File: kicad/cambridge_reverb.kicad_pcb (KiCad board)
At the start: 2 copper layers, 190 x 115 mm, 113 parts, among them IC1 TL072CP, IC2 TL072CP, Q1 MMBF5457, Q2 MMBF5457, T1 reuse / AnTek AS-0524, U1 LM317T

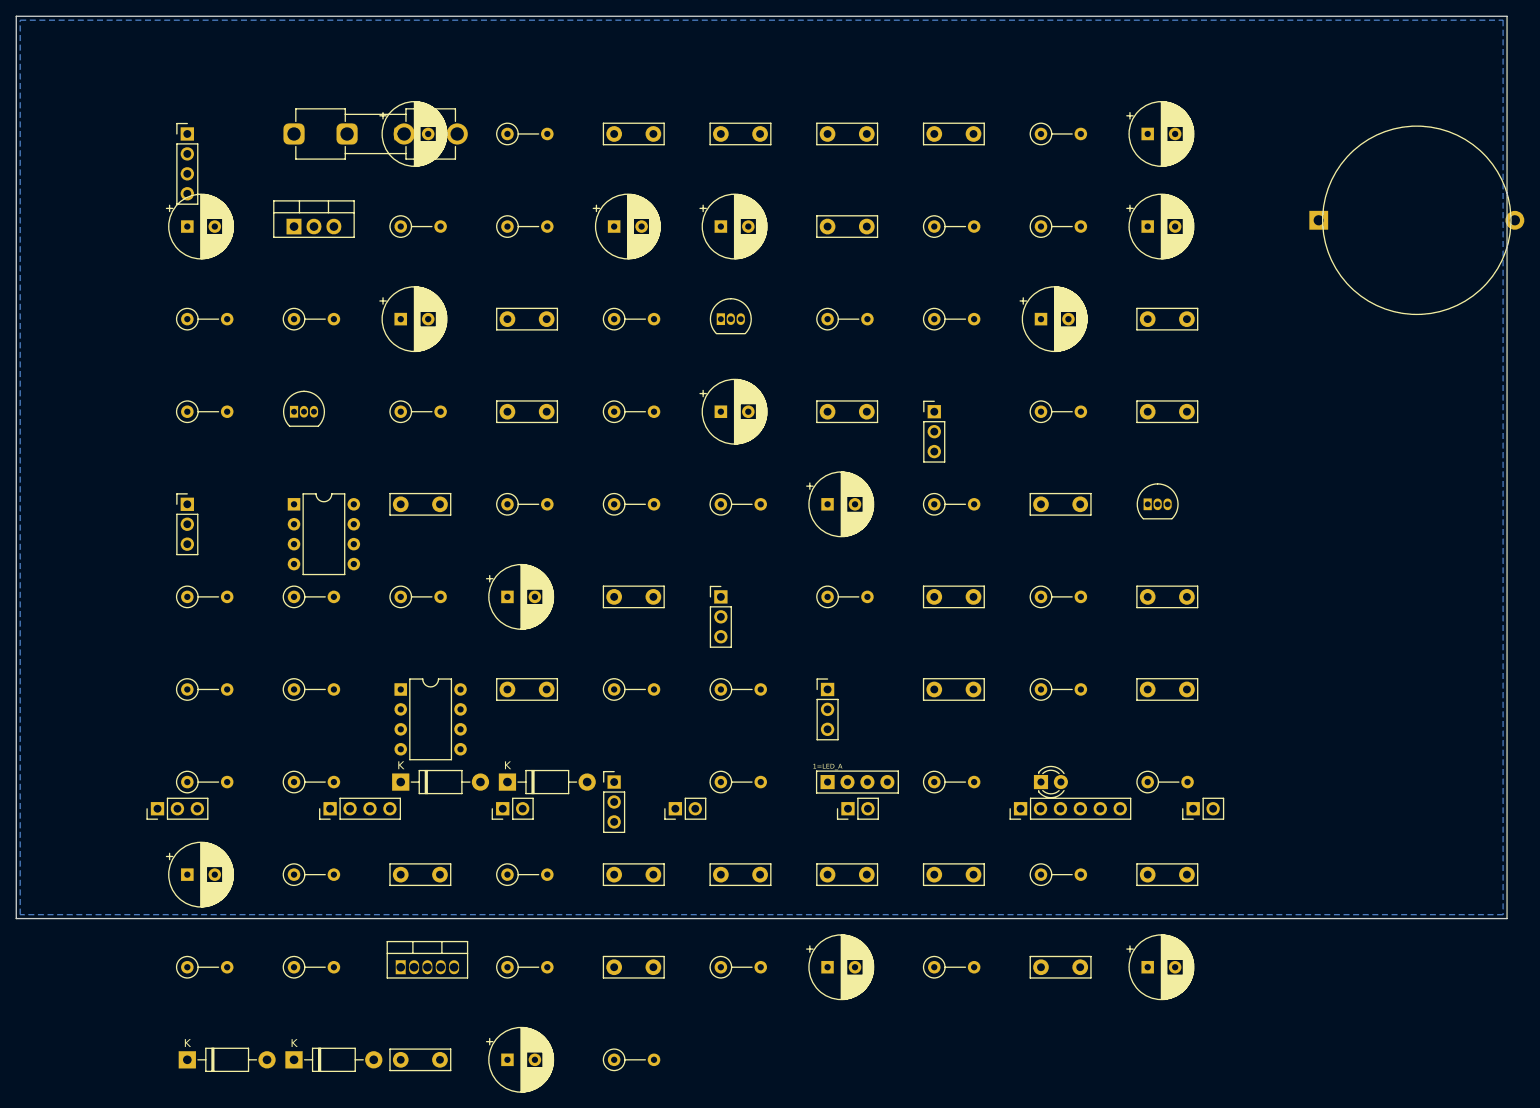
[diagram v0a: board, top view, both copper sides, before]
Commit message: Datasheet footprints, floor-plan placement, headless autoroute (144/145, DRC 0)
PCB-AUDIT s1 fixes with datasheet-derived project footprints:
- TO-220-5_Vertical_P1.70mm_LM1875 (TI NDH0005D): 1.45 mm pads on the 1.1 mm
  drill -> 0.175 mm annular (was 0.0875, 5 DRC errors); pad-local 0.2 mm clearance
- Bridge_KBP_P3.81mm (Diodes DS39310 KBP404G-KBP410G, pins + ~ ~ -); bridge
  symbol renumbered to the physical order; errata #3 updated (KBU needs a swap)
- value-aware CP/R sizing (real can sizes for 4700/2200/1000 uF, 5 W / 1 W
  resistors, fat pads on the 0R speaker return); Part 4 wire pads for all
  off-board wiring (2.0 mm/1.2 mm signal, 3.0 mm/1.5 mm speaker + transformer)
- VRAW/AC1/AC2 moved into the HighCurrent net class (errata #11)

gen_pcb.py now places to the Part 5 floor plan: balanced columns (Input/Preamp
with Tone stacked below | Reverb/Trem/MRB | Power Amp | PSU), signal order inside
zones with serpentine shelves, LM1875/LM317 on the top edge with the 10 mm
keep-out, wiring edge along the bottom, 4x M3 holes, two locked 0.9 mm escape
stubs off the LM1875 pins 4/5 (a 1.5/2.5 mm trace cannot enter a 1.70 mm pitch).
DRC before routing: 0 errors, 0 warnings.

route_board.py: pcbnew DSN export -> Freerouting -> SES import -> pour refill.
Freerouting 2.1.0 ignores every pass/timeout limit in CLI mode and only writes
output at 0 unrouted (and its MT router crashed), so the script drives 1.9.0
under xvfb-run and injects autoroute_settings (bottom layer 6x cost, via 80) so
the GND pour stays whole. Committed board: 144/145 connections routed, 0 DRC
violations (--severity-all), 26 vias, 351 mm on the bottom vs 3.7 m on top; the
one open PA_OUT link (blocked by R_bias1) is documented as a GUI finish.

Chassis-fit figure corrected: the old 48-53 % / 82-90 % densities counted hidden
text boxes; text-less it is ~33 % on 190x115 and ~56 % on 155x90.

Docs: PCB-NOTES/PCB-AUDIT rewritten, README, CHANGELOG, errata #3/#11,
SOURCES (package drawings), Part 10, kicad RE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
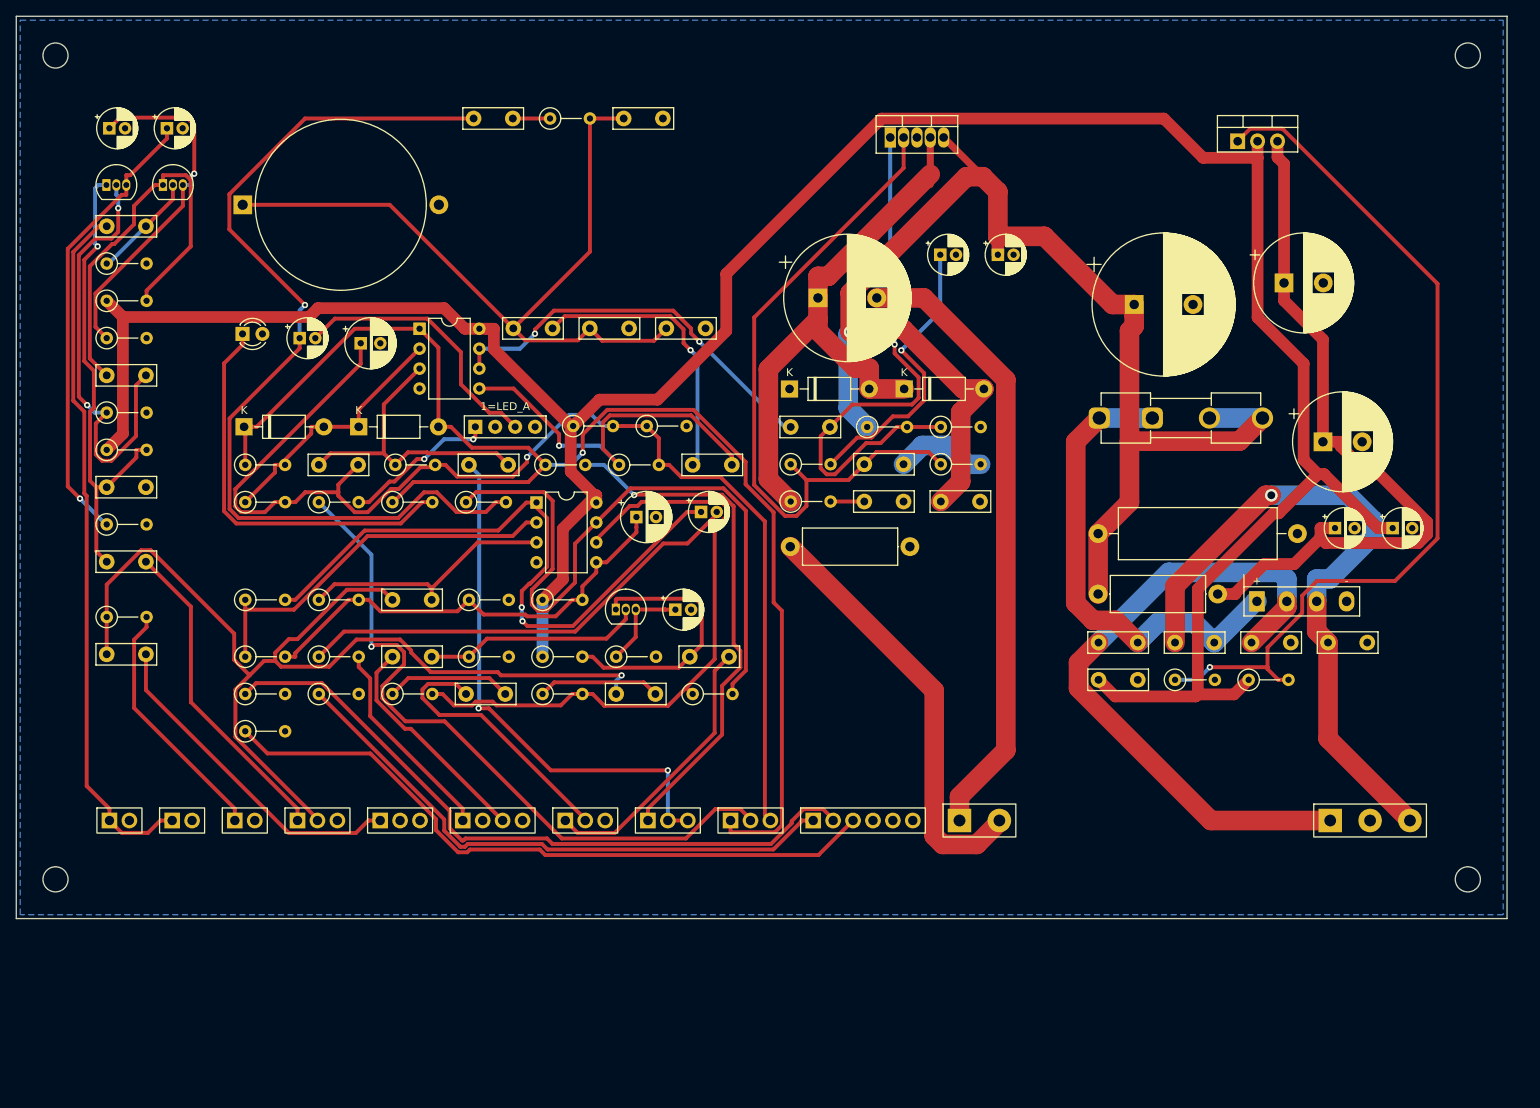
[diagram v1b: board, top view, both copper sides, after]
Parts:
- removed the C_dc_blk at (21.8, 109.4)
- removed the C_gain at (103.4, 121.2)
- removed the C_main at (49.0, 15.0)
- removed the C_out at (144.2, 121.2)
- removed the C_rec_byp at (62.6, 74.0)
- removed the C_reg_in at (76.2, 26.8)
- removed the C_vbr at (144.2, 26.8)
- removed the C_vbt at (49.0, 38.6)
- removed the IC_PA at (49.0, 121.2)
- removed the POT_DPT at (76.2, 97.6)
- removed the POT_REV at (89.8, 74.0)
- removed the POT_SPD at (103.4, 85.8)
- removed the POT_TONE at (21.8, 62.2)
- removed the POT_VOL at (117.0, 50.4)
- removed the R_27V at (130.6, 15.0)
- removed the R_bleed at (62.6, 15.0)
- removed the R_spk_rtn at (76.2, 133.0)
- added C_dc_blk: 10uF, CP_Radial_D5.0mm_P2.00mm, F.Cu at (36.1, 41.0)
- added C_gain: 22uF/25V, CP_Radial_D5.0mm_P2.00mm, F.Cu at (117.8, 30.4)
- added C_main: 4700uF/50V, CP_Radial_D18.0mm_P7.50mm, F.Cu at (142.5, 36.7)
- added C_out: 2200uF/35V, CP_Radial_D16.0mm_P7.50mm, F.Cu at (102.2, 35.9)
- added C_rec_byp: 10uF, CP_Radial_D5.0mm_P2.00mm, F.Cu at (84.0, 75.6)
- added C_reg_in: 10uF/50V, CP_Radial_D5.0mm_P2.50mm, F.Cu at (168.1, 65.2)
- added C_vbr: 47uF/25V, CP_Radial_D6.3mm_P2.50mm, F.Cu at (79.0, 63.8)
- added C_vbt: 47uF/25V, CP_Radial_D6.3mm_P2.50mm, F.Cu at (43.9, 41.7)
- added H1: MountingHole_3.2mm_M3, MountingHole_3.2mm_M3, F.Cu at (5.00, 5.00)
- added H2: MountingHole_3.2mm_M3, MountingHole_3.2mm_M3, F.Cu at (185.0, 5.00)
- added H3: MountingHole_3.2mm_M3, MountingHole_3.2mm_M3, F.Cu at (5.00, 110.0)
- added H4: MountingHole_3.2mm_M3, MountingHole_3.2mm_M3, F.Cu at (185.0, 110.0)
- added IC_PA: LM1875T, TO-220-5_Vertical_P1.70mm_LM1875, F.Cu at (111.4, 15.4)
- added POT_DPT: 100k lin, WirePad_1x03_P2.54mm_D1.2mm, F.Cu at (91.0, 102.5)
- added POT_REV: reuse, WirePad_1x03_P2.54mm_D1.2mm, F.Cu at (70.0, 102.5)
- added POT_SPD: 500k lin, WirePad_1x03_P2.54mm_D1.2mm, F.Cu at (80.5, 102.5)
- added POT_TONE: 100k lin, WirePad_1x03_P2.54mm_D1.2mm, F.Cu at (46.4, 102.5)
- added POT_VOL: 250k log, WirePad_1x03_P2.54mm_D1.2mm, F.Cu at (35.8, 102.5)
- added R_27V: 100R/1W, R_Axial_DIN0414_L11.9mm_D4.5mm_P15.24mm_Horizontal, F.Cu at (137.9, 73.6)
- added R_bleed: 10k/5W, R_Axial_Power_L20.0mm_W6.4mm_P25.40mm, F.Cu at (137.9, 65.9)
- added R_spk_rtn: 0R, R_Axial_DIN0414_L11.9mm_D4.5mm_P15.24mm_Horizontal, F.Cu at (98.7, 67.6)
- BR1: footprint PinHeader_1x04_P2.54mm_Vertical -> Bridge_KBP_P3.81mm
- C_byp2, C_rev1, C_s1, C_s2: footprint CP_Radial_D8.0mm_P3.50mm -> CP_Radial_D5.0mm_P2.00mm
- C_filt1, C_filt2: footprint CP_Radial_D8.0mm_P3.50mm -> CP_Radial_D12.5mm_P5.00mm
- C_reg_out1: footprint CP_Radial_D8.0mm_P3.50mm -> CP_Radial_D5.0mm_P2.50mm
- FS1: footprint PinHeader_1x06_P2.54mm_Vertical -> WirePad_1x06_P2.54mm_D1.2mm
- J_IN1, J_IN2, J_IN3: footprint PinHeader_1x02_P2.54mm_Vertical -> WirePad_1x02_P2.54mm_D1.2mm
- LS1: footprint PinHeader_1x02_P2.54mm_Vertical -> WirePad_1x02_P5.08mm_D1.5mm
- REV1: footprint PinHeader_1x04_P2.54mm_Vertical -> WirePad_1x04_P2.54mm_D1.2mm
- T1: footprint PinHeader_1x03_P2.54mm_Vertical -> WirePad_1x03_P5.08mm_D1.5mm
- moved T1 149.5 mm to (167.5, 102.5), turned to 0 degrees
- moved BR1 148.8 mm to (158.1, 74.6)
- moved C_filt2 147.3 mm to (166.5, 54.2)
- moved L1 137.2 mm to (28.9, 24.0)
- moved C_cut 136.2 mm to (11.5, 81.3)
- moved C_cpl12 132.9 mm to (11.5, 45.8)
- moved D1 125.1 mm to (113.2, 47.5)
- moved R_reg1 122.5 mm to (157.1, 84.6)
- moved R_fx_pad 121.9 mm to (11.5, 76.6)
- moved C_s1 121.2 mm to (11.9, 14.3)
- moved U1 120.8 mm to (155.7, 15.9)
- moved C_byp2 120.1 mm to (125.1, 30.4)
- moved LED_rate 116.7 mm to (28.8, 40.5)
- moved R_bias1 110.7 mm to (108.5, 52.3)
- moved C_lfo2 109.4 mm to (38.6, 57.2)
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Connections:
- BR1 pad 1: AC1 -> VRAW
- BR1 pad 2: VRAW -> AC1
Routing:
- net +17V: track 0.00 -> 344.4 mm
- net +33V5: track 0.00 -> 180.7 mm, vias 0 -> 1
- net LFO_OUT: track 0.00 -> 172.2 mm, vias 0 -> 1
- net VBIAS_T: track 0.00 -> 154.9 mm, vias 0 -> 1
- net TONE_OUT: track 0.00 -> 135.5 mm, vias 0 -> 1
- net TREM_OUT: track 0.00 -> 121.8 mm, vias 0 -> 1
- net ADJ17: track 0.00 -> 113.9 mm, vias 0 -> 1
- net MRB_T: track 0.00 -> 98.2 mm
- net VREG_IN: track 0.00 -> 93.7 mm
- net DPT_W: track 0.00 -> 89.4 mm, vias 0 -> 1
- net GUITAR_IN: track 0.00 -> 89.3 mm
- net BLEND: track 0.00 -> 88.6 mm
- net FS_TREM: track 0.00 -> 88.2 mm
- net PA_OUT: track 0.00 -> 87.5 mm
- net FS_MRB: track 0.00 -> 86.9 mm
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
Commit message: Add 26 labelled bench test points (schematic + BOM + silk) and re-route
Test points follow the Part 5 bring-up order: rails (VRAW, +33V5, VREG_IN,
+17V), JFET drains Q1D/Q2D/QRD (the errata #15 bias trim), the VBIAS_R/VBIAS_T
mid-rail refs, every inter-stage node (PREAMP_OUT, TONE_OUT, BLEND, TREM_OUT,
MRB_OUT, PA_IN), tank drive/return, LFO, PA_BIAS/PA_OUT/SPK_P, and a GND pin
per zone for the probe clip.

- gen_kicad.py: one-pin TP symbol; TEST_POINTS table; add_test_points() puts
  them on their sheets so they are in the netlist and the BOM (one order line)
- footprint TestPoint_THT_D2.0mm_Label: 2.0 mm pad / 1.0 mm drill for a header
  pin or wire loop; the footprint VALUE (= net alias) prints on F.SilkS
- gen_pcb.py: test-point strip across the top of each zone; the effects column
  is now two stacked zones (tremolo+MRB above, reverb below next to its tank
  pads) so each block's points sit right above its parts; stacked-zone gap 2 mm
- PCB-NOTES.md: test-point table with expected values (Part 3 troubleshooting,
  Part 2 set-up, ngspice) and the bring-up sequence
- Re-routed (Freerouting 1.9.0, B.Cu x7, via 60): 161/166 connections, 0 DRC
  violations, 54 vias; the five open links are listed for a GUI finish

Co-Authored-By: Claude Fable 5.1 <noreply@anthropic.com>
Claude-Session: https://claude.ai/code/session_01Vk8HkvCugxFpQsBPVnNT2H
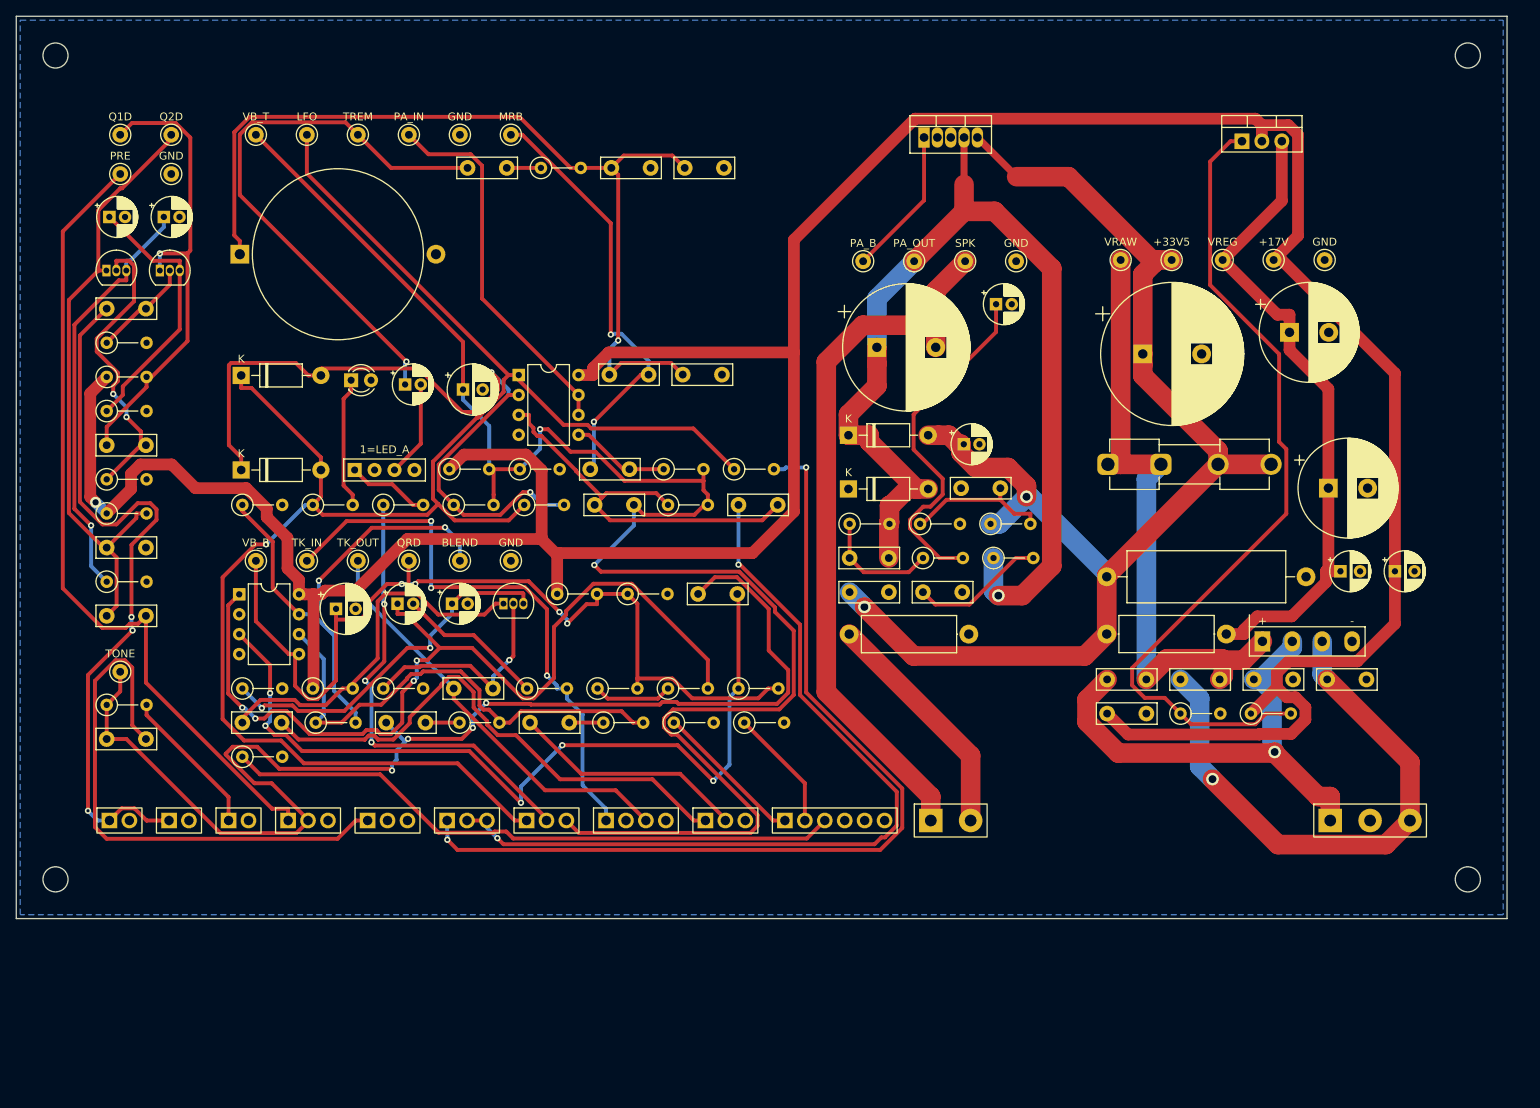
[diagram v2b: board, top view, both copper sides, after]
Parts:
- added TP_17V: +17V, TestPoint_THT_D2.0mm_Label, F.Cu at (160.3, 31.1)
- added TP_33V5: +33V5, TestPoint_THT_D2.0mm_Label, F.Cu at (147.3, 31.1)
- added TP_BLEND: BLEND, TestPoint_THT_D2.0mm_Label, F.Cu at (56.5, 69.4)
- added TP_GND_PA: GND, TestPoint_THT_D2.0mm_Label, F.Cu at (127.4, 31.2)
- added TP_GND_PRE: GND, TestPoint_THT_D2.0mm_Label, F.Cu at (19.8, 20.1)
- added TP_GND_PSU: GND, TestPoint_THT_D2.0mm_Label, F.Cu at (166.8, 31.1)
- added TP_GND_REV: GND, TestPoint_THT_D2.0mm_Label, F.Cu at (63.0, 69.4)
- added TP_GND_TREM: GND, TestPoint_THT_D2.0mm_Label, F.Cu at (56.5, 15.1)
- added TP_LFO: LFO, TestPoint_THT_D2.0mm_Label, F.Cu at (37.0, 15.1)
- added TP_MRB_OUT: MRB, TestPoint_THT_D2.0mm_Label, F.Cu at (63.0, 15.1)
- added TP_PA_BIAS: PA_B, TestPoint_THT_D2.0mm_Label, F.Cu at (107.9, 31.2)
- added TP_PA_IN: PA_IN, TestPoint_THT_D2.0mm_Label, F.Cu at (50.0, 15.1)
- added TP_PA_OUT: PA_OUT, TestPoint_THT_D2.0mm_Label, F.Cu at (114.4, 31.2)
- added TP_PRE_OUT: PRE, TestPoint_THT_D2.0mm_Label, F.Cu at (13.2, 20.1)
- added TP_Q1D: Q1D, TestPoint_THT_D2.0mm_Label, F.Cu at (13.2, 15.1)
- added TP_Q2D: Q2D, TestPoint_THT_D2.0mm_Label, F.Cu at (19.8, 15.1)
- added TP_QRD: QRD, TestPoint_THT_D2.0mm_Label, F.Cu at (50.0, 69.4)
- added TP_SPK: SPK, TestPoint_THT_D2.0mm_Label, F.Cu at (120.9, 31.2)
- added TP_TANK_IN: TK_IN, TestPoint_THT_D2.0mm_Label, F.Cu at (37.0, 69.4)
- added TP_TANK_OUT: TK_OUT, TestPoint_THT_D2.0mm_Label, F.Cu at (43.5, 69.4)
- added TP_TONE_OUT: TONE, TestPoint_THT_D2.0mm_Label, F.Cu at (13.2, 83.5)
- added TP_TREM_OUT: TREM, TestPoint_THT_D2.0mm_Label, F.Cu at (43.5, 15.1)
- added TP_VBIAS_R: VB_R, TestPoint_THT_D2.0mm_Label, F.Cu at (30.5, 69.4)
- added TP_VBIAS_T: VB_T, TestPoint_THT_D2.0mm_Label, F.Cu at (30.5, 15.1)
- added TP_VRAW: VRAW, TestPoint_THT_D2.0mm_Label, F.Cu at (140.8, 31.1)
- added TP_VREG_IN: VREG, TestPoint_THT_D2.0mm_Label, F.Cu at (153.8, 31.1)
- moved R_fs_trem 63.7 mm to (92.8, 90.0)
- moved C_rev4 57.6 mm to (28.8, 90.0)
- moved R_drv1 55.1 mm to (83.1, 85.7)
- moved R_drvbias 54.7 mm to (92.0, 85.7)
- moved R_mixfb 48.2 mm to (38.2, 90.0)
- moved R_rec2 47.8 mm to (28.8, 85.7)
- moved R_fs_rev 45.4 mm to (83.8, 90.0)
- moved R_drv2 45.1 mm to (74.1, 85.7)
- moved C_rev1 40.4 mm to (48.6, 74.9)
- moved C_vbr 40.0 mm to (40.7, 75.5)
- moved IC1 39.7 mm to (28.4, 73.7)
- moved C_drvin 39.0 mm to (86.9, 73.6)
- moved R_lfo_fb1 35.9 mm to (64.7, 62.3)
- moved C_lfo2 35.5 mm to (73.7, 62.3)
- moved R_lfo1 35.1 mm to (83.1, 62.3)
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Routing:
- net +17V: track 344.4 -> 432.1 mm, vias 0 -> 1
- net DRVP: track 32.7 -> 106.0 mm, vias 0 -> 5
- net FS_TREM: track 88.2 -> 15.7 mm
- net PA_INV: track 86.4 -> 15.2 mm
- net LFO_N: track 33.3 -> 97.6 mm, vias 0 -> 2
- net VBIAS_T: track 154.9 -> 217.9 mm, vias 1 -> 2
- net PREAMP_OUT: track 41.0 -> 103.9 mm
- net FS_REV: track 73.9 -> 19.3 mm
- net VBIAS_R: track 58.3 -> 111.8 mm, vias 0 -> 4
- net LFO_OUT: track 172.2 -> 225.5 mm
- net SPD_A: track 66.4 -> 117.4 mm, vias 1 -> 2
- net TREM_OUT: track 121.8 -> 72.8 mm
- net PA_OUT: track 87.5 -> 134.4 mm, vias 0 -> 1
- net TANK_IN: track 26.4 -> 73.2 mm, vias 0 -> 3
- net TKDRV: track 58.5 -> 19.0 mm
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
